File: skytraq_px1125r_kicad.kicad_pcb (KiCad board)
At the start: 4 copper layers, 36 x 36 mm, 47 parts, among them J1 JST_GH_1.25_6P, J2 SMA, J3 JST_GH_1.25_6P, J5 Conn_01x06, J7 Conn_01x06, U1 Skytraq_PX1125R, U2 RV-3032, U3 LIS3MDL, U6 AMS1117-3.3

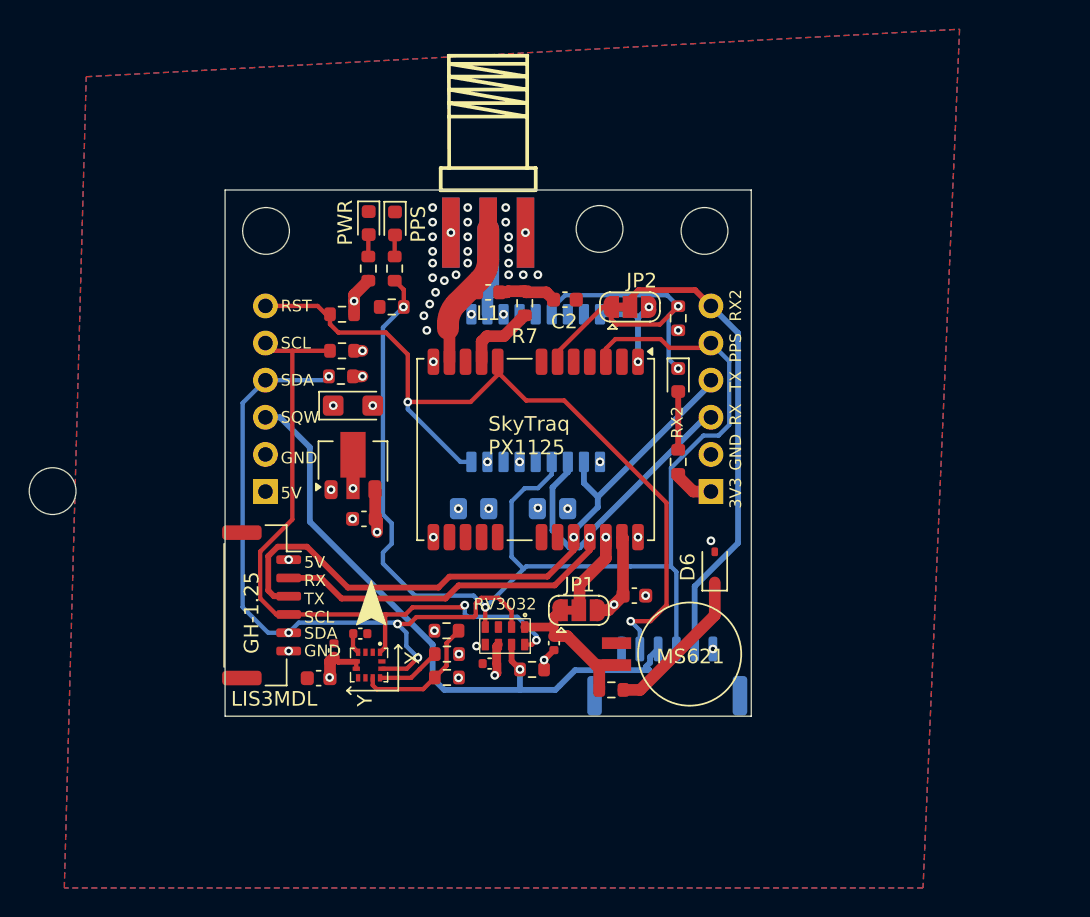
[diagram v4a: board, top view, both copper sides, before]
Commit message: one more M3 hole
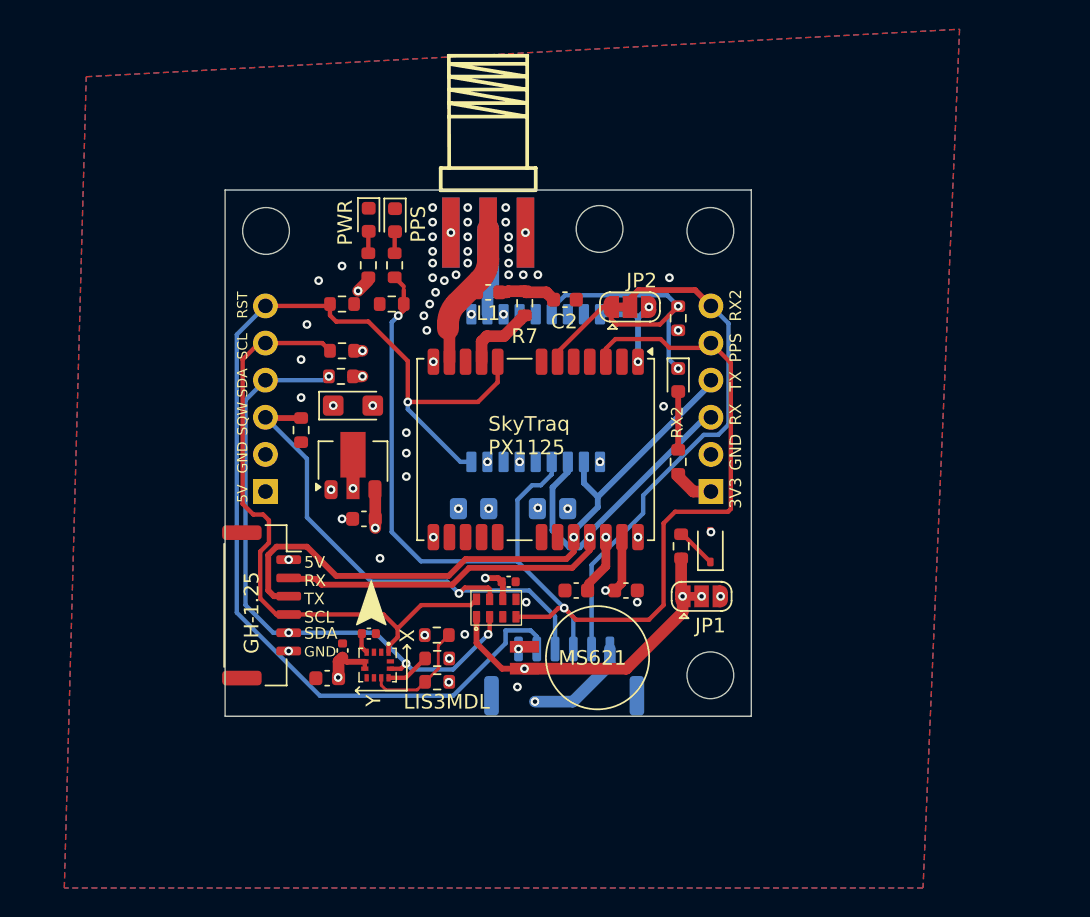
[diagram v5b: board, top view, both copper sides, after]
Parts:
- C3: value 100nF -> 10uF; footprint Capacitor_SMD:C_0402_1005Metric -> Capacitor_SMD:C_0603_1608Metric
- U5: value ~ -> SkyTraq_PX1105
- moved H2 43.0 mm to (123.2, 73.2)
- moved H4 23.2 mm to (92.8, 42.6)
- moved R2 22.8 mm to (95.2, 56.4), turned to -90 degrees
- moved R4 10.9 mm to (121.2, 64.4), turned to -90 degrees
- moved JP1 8.45 mm to (122.6, 67.8)
- moved J3 7.05 mm to (113.2, 73.2)
- moved BT1 6.30 mm to (110.5, 72.0)
- moved C10 5.75 mm to (109.4, 66.8), turned to 0 degrees
- moved C3 3.91 mm to (114.0, 67.4), turned to 180 degrees
- moved U2 1.99 mm to (108.5, 68.6), turned to 0 degrees
- moved D6 1.43 mm to (123.2, 64.4)
- moved R8 0.73 mm to (104.5, 73.7)
- moved R11 0.73 mm to (104.5, 72.0)
- moved R9 0.73 mm to (104.5, 70.5)
- moved R1 0.70 mm to (98.0, 47.8)
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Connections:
- C3 pad 1: /VBAT -> /GPS_V_BCKP
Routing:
- net GPS_RST: track 56.9 -> 77.2 mm, vias 2 -> 1
- net /VBAT: track 10.8 -> 22.0 mm, vias 0 -> 2
- net /+5V: track 56.1 -> 47.2 mm
- net RTC_CLK: track 44.1 -> 35.7 mm
- net Net-(D6-K): track 10.6 -> 2.79 mm
- net SDA: track 49.1 -> 42.8 mm
- net /GPS_V_BCKP: track 18.6 -> 24.8 mm, vias 3 -> 4
- net SCL: track 47.5 -> 42.8 mm, vias 2 -> 0
- net +3V3: track 113.1 -> 109.8 mm, vias 14 -> 15
- net BOOT/GPS_RX2: track 32.3 -> 35.2 mm
- net Net-(U3-SDO/SA1): track 9.36 -> 7.74 mm
- net GND: track 1.60 -> 0.00 mm, vias 43 -> 56
- net Net-(U3-~{CS}): track 4.42 -> 3.05 mm
- net GPS_RX: track 43.8 -> 43.0 mm
- net GPS_PPS: track 86.1 -> 85.3 mm
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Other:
- board text removed: "RV3032"

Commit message: 36x36 for flight controllers
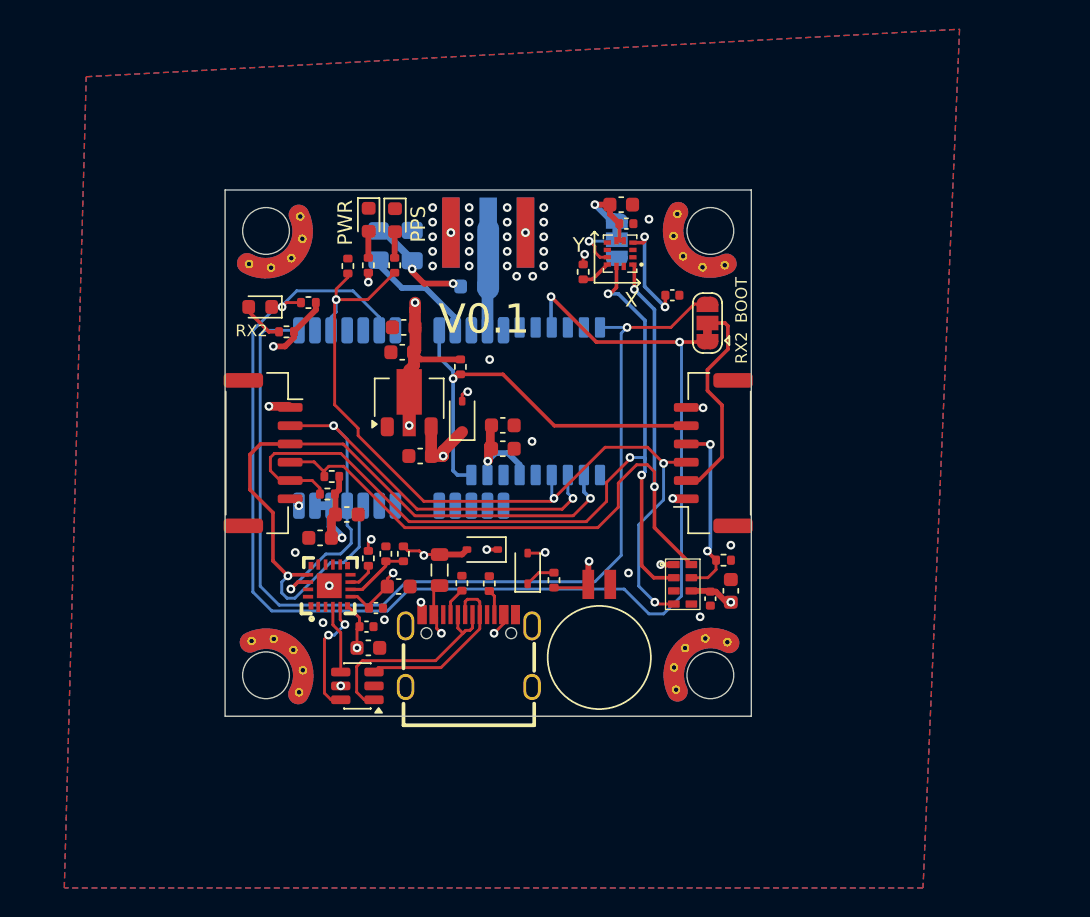
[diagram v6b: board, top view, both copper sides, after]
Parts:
- removed J7: Conn_01x06, Connector_PinHeader_2.54mm:PinHeader_1x06_P2.54mm_Vertical
- removed R8, R9: 0, Resistor_SMD:R_0603_1608Metric
- added C11: 10uF, Capacitor_SMD:C_0603_1608Metric, F.Cu at (101.9, 67.1)
- added C12: 100nF, Capacitor_SMD:C_0402_1005Metric, F.Cu at (100.3, 68.6)
- added C13: 10uF, Capacitor_SMD:C_0603_1608Metric, F.Cu at (102.2, 49.4)
- added C14: 10uF, Capacitor_SMD:C_0603_1608Metric, F.Cu at (99.8, 71.3)
- added C15: 100nF, Capacitor_SMD:C_0402_1005Metric, F.Cu at (99.7, 69.9)
- added C16: 10uF, Capacitor_SMD:C_0603_1608Metric, F.Cu at (124.6, 67.4)
- added D4: D_Schottky, Diode_SMD:D_SOD-323, F.Cu at (107.6, 64.6)
- added D5: D_Schottky, Diode_SMD:D_SOD-323, F.Cu at (106.2, 55.5)
- added FB2: FerriteBead, Inductor_SMD:L_0805_2012Metric, F.Cu at (104.7, 66.0)
- added R15: 1k, Resistor_SMD:R_0402_1005Metric, F.Cu at (99.8, 65.2)
- added R16: 22k, Resistor_SMD:R_0402_1005Metric, F.Cu at (102.2, 64.9)
- added R17: 47k, Resistor_SMD:R_0402_1005Metric, F.Cu at (101.0, 64.9)
- added R20: 5.1k, Resistor_SMD:R_0402_1005Metric, F.Cu at (106.2, 66.9)
- added R21: 5.1k, Resistor_SMD:R_0402_1005Metric, F.Cu at (108.1, 66.9)
- added U4: CP2102N-A02-GQFN20R, footprint:QFN-20_L3.0-W3.0-P0.50-BL-EP1.7_EFM8BB21F16G, F.Cu at (97.1, 67.1)
- added U7: USBLC6-2SC6, Package_TO_SOT_SMD:SOT-23-6, F.Cu at (99.1, 73.9)
- C2: footprint Capacitor_SMD:C_0603_1608Metric -> Capacitor_SMD:C_0805_2012Metric_Pad1.18x1.45mm_HandSolder; moved to B.Cu
- C4: value 100nF -> 10uF; footprint Capacitor_SMD:C_0805_2012Metric_Pad1.18x1.45mm_HandSolder -> Capacitor_SMD:C_0603_1608Metric; moved to F.Cu
- C5: footprint Capacitor_SMD:C_0805_2012Metric_Pad1.18x1.45mm_HandSolder -> Capacitor_SMD:C_0603_1608Metric; moved to F.Cu
- C6: value 22uF -> 10uF; footprint Capacitor_Tantalum_SMD:CP_EIA-3216-18_Kemet-A -> Capacitor_SMD:C_0603_1608Metric
- H1, H2, H3, H4: value MountingHole -> MountingHole_Pad; footprint MountingHole:MountingHole_3.2mm_M3 -> MyFootprints:MountingHole_3.2mm_M3_Pad
- J2: footprint footprint:SMA-SMD_BWSMA-KE-P001_Symmetric -> footprint:SMA-SMD_BWSMA-KE-P001; moved to B.Cu
- J3: moved to F.Cu
- J5: value Conn_01x06 -> USB_C_Receptacle_USB2.0_16P; footprint Connector_PinHeader_2.54mm:PinHeader_1x06_P2.54mm_Vertical -> footprint:USB-C_SMD-TYPE-C-31-M-12_1; moved to F.Cu
- JP1, L1, U1: moved to B.Cu
- R1, R10, R11, R12, R13, R14, R2, R3, R4, R5, R6: footprint Resistor_SMD:R_0603_1608Metric -> Resistor_SMD:R_0402_1005Metric
- R7: footprint Resistor_SMD:R_0603_1608Metric -> Resistor_SMD:R_0805_2012Metric_Pad1.20x1.40mm_HandSolder; moved to B.Cu
- moved C23 38.1 mm to (117.1, 41.0), turned to 180 degrees
- moved H1 38.1 mm to (92.8, 73.2), turned to -30 degrees
- moved C8 35.1 mm to (117.5, 42.3), turned to 0 degrees
- moved U3 32.7 mm to (117.0, 44.3), turned to 90 degrees
- moved C9 31.1 mm to (120.6, 47.2)
- moved R2 30.2 mm to (124.1, 65.3), turned to 0 degrees
- moved D3 29.0 mm to (92.4, 48.0), turned to 180 degrees
- moved R11 28.3 mm to (114.5, 45.6), turned to 90 degrees
- moved R13 28.2 mm to (94.2, 49.7), turned to 180 degrees
- moved R3 25.3 mm to (95.7, 47.7), turned to 0 degrees
- moved JP1 25.1 mm to (116.8, 43.4), turned to -90 degrees
- moved C1 19.8 mm to (98.3, 62.2)
- moved J3 18.3 mm to (123.4, 58.0), turned to 90 degrees
- moved C3 17.9 mm to (96.5, 63.8)
- moved J5 17.7 mm to (106.7, 71.5)
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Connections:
- net BOOT/GPS_RX2 renamed /BOOT/GPS_RX2
- net GPS_PPS renamed /GPS_PPS
- net GPS_RX renamed /GPS_RX
- net GPS_TX renamed /GPS_TX
- C3 pad 1: /GPS_V_BCKP -> +3V3
- C4 pad 1: /GPS_V_BCKP -> GND
- C4 pad 2: GND -> +3V3
- C5 pad 1: +3V3 -> GND
- C5 pad 2: GND -> +3V3
- C6 pad 1: +3V3 -> GND
- C6 pad 2: GND -> +3V3
- J1 pad 1: /+5V -> /+5V_IN
- J3 pad 1: /+5V -> /+5V_IN
- J3 pad 4: RTC_CLK -> /RTC_CLK
- J3 pad 5: GPS_RST -> /GPS_RST
- JP1 pad 1: /VBAT -> +3V3
- JP1 pad 2: /GPS_V_BCKP -> Net-(JP1-C)
- JP1 pad 3: +3V3 -> GND
- R1 pad 2: GPS_RST -> /GPS_RST
- R2 pad 1: RTC_CLK -> /RTC_CLK
- U1 pad 22: /GPS_V_BCKP -> +3V3
- U1 pad 8: GPS_RST -> /GPS_RST
- U2 pad 7: RTC_CLK -> /RTC_CLK
- U3 pad 9: Net-(U3-SDO/SA1) -> Net-(JP1-C)
- U5 pad 6: /GPS_V_BCKP -> +3V3
- U5 pad 9: GPS_RST -> /GPS_RST
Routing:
- net GPS_RST: track 77.2 -> 0.00 mm, vias 1 -> 0
- net /GPS_RX2: track 26.2 -> 94.7 mm, vias 2 -> 3
- net /GPS_BOOT: track 6.76 -> 70.4 mm, vias 2 -> 1
- net RTC_CLK: track 35.7 -> 0.00 mm, vias 1 -> 0
- net /+5V_IN: track 0.00 -> 34.5 mm, vias 0 -> 3
- net /+5V: track 47.2 -> 13.4 mm, vias 3 -> 2
- net /GPS_RST: track 0.00 -> 28.9 mm, vias 0 -> 1
- net /GPS_PPS: track 85.3 -> 59.1 mm, vias 2 -> 4
- net /GPS_V_BCKP: track 24.8 -> 0.00 mm, vias 4 -> 0
- net /BOOT/GPS_RX2: track 35.2 -> 14.6 mm
- net SDA: track 42.8 -> 60.4 mm, vias 4 -> 3
- net Net-(U7-VBUS): track 0.00 -> 17.1 mm, vias 0 -> 3
- net Net-(J5-D--PadA7): track 0.00 -> 14.8 mm
- net /RTC_CLK: track 0.00 -> 12.5 mm, vias 0 -> 2
- net Net-(J5-D+-PadA6): track 0.00 -> 12.3 mm
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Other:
- board text added: "BOOT"
- board text added: "PX1105"
- board text added: "PX1125"
- board text removed: "5V"
- board text removed: "GH-1.25"
- board text removed: "LIS3MDL"
- board text removed: "MS621"
- board text removed: "RST"
- board text removed: "RX"
- board text removed: "SCL"
- board text removed: "SDA"
- board text removed: "SQW"
- board text removed: "SkyTraq PX1105"
- board text removed: "SkyTraq PX1125"
- board text removed: "TX"
